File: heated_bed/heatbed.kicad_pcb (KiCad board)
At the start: 2 copper layers, 249.6 x 227 mm, 10 parts, among them P1 CONN_4

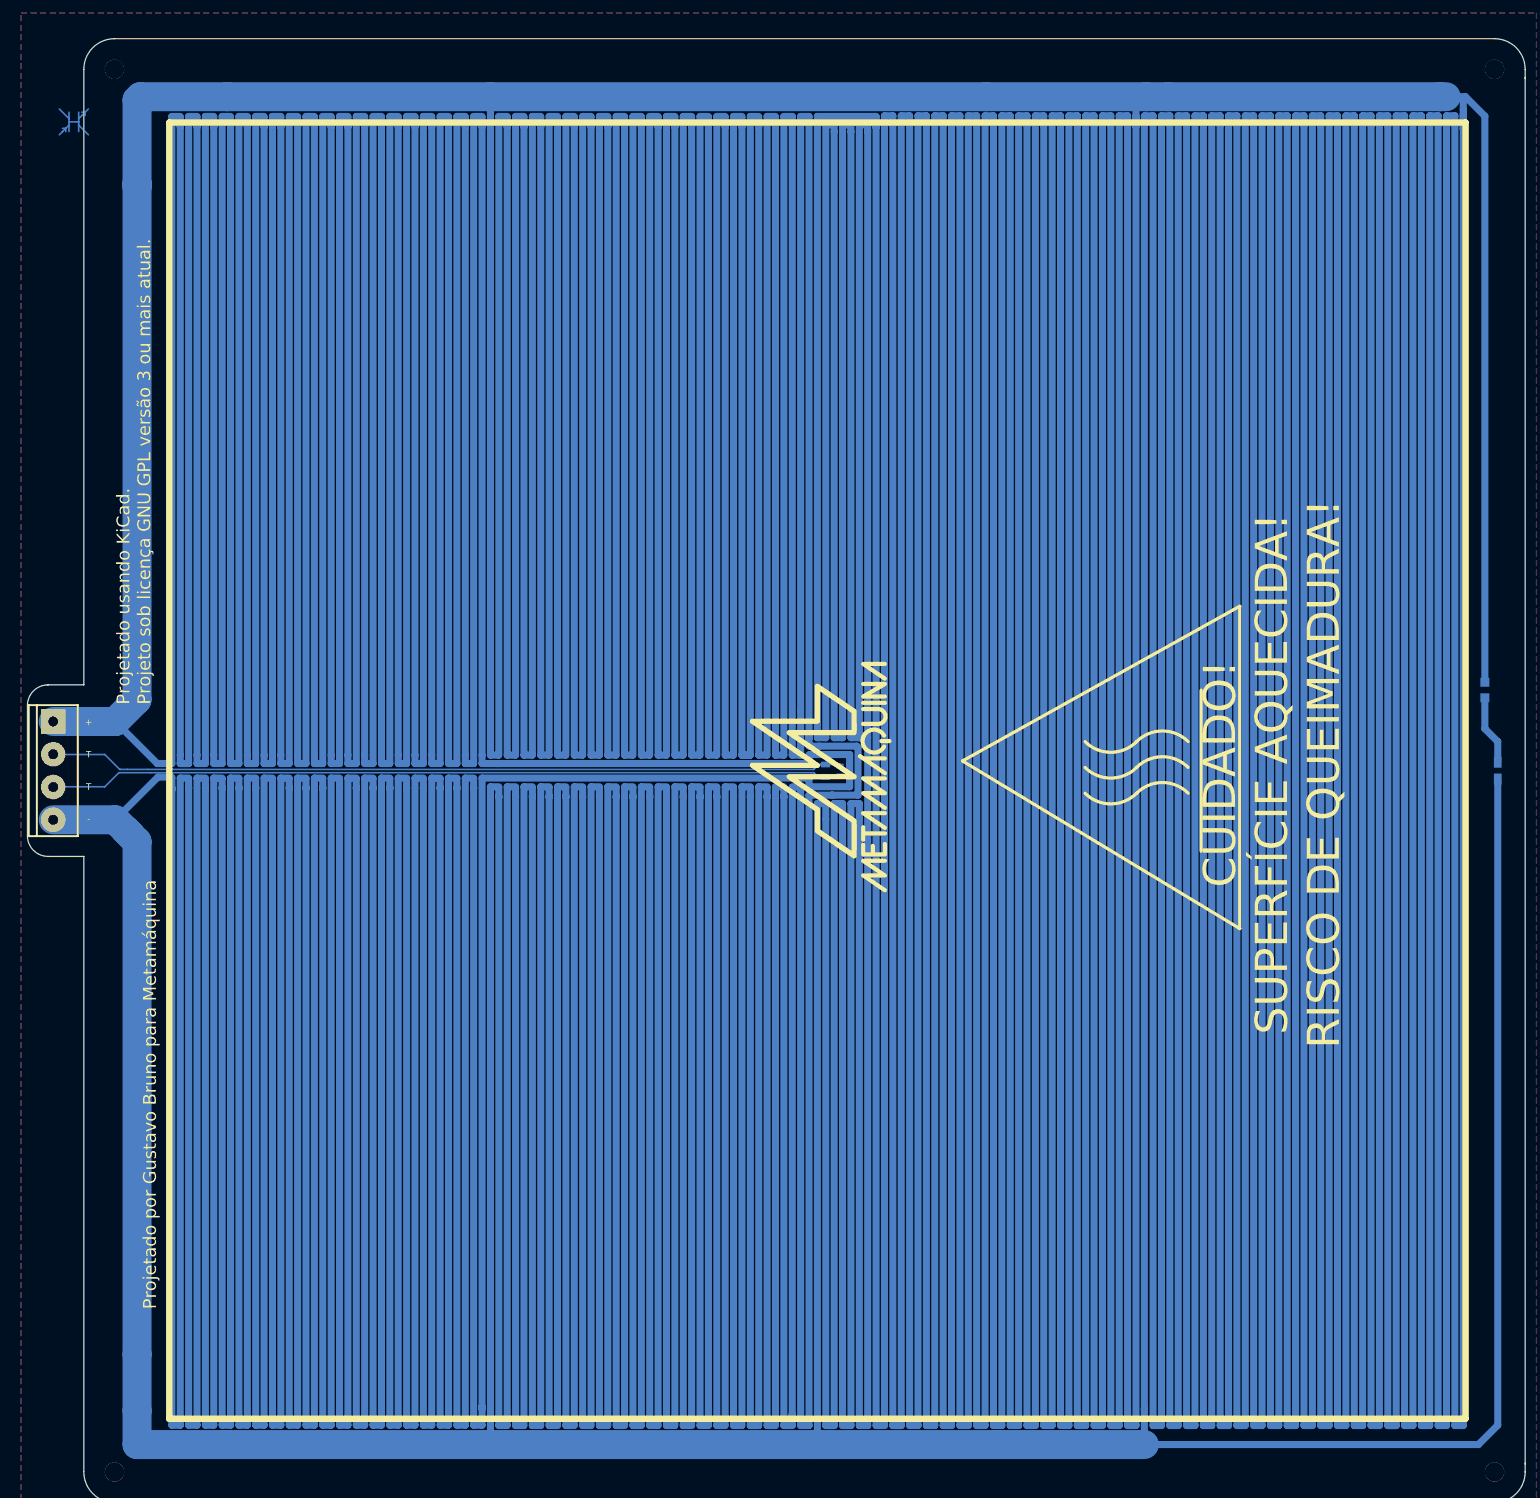
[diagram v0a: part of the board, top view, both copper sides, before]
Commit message: Correcoes apos prototipo fresado:
Bug que colava duas trilhas
Led avancado
Linha de distribuicao mais proxima
Textos do silk realinhados
Remoca do desenho de quente
Nome da placa
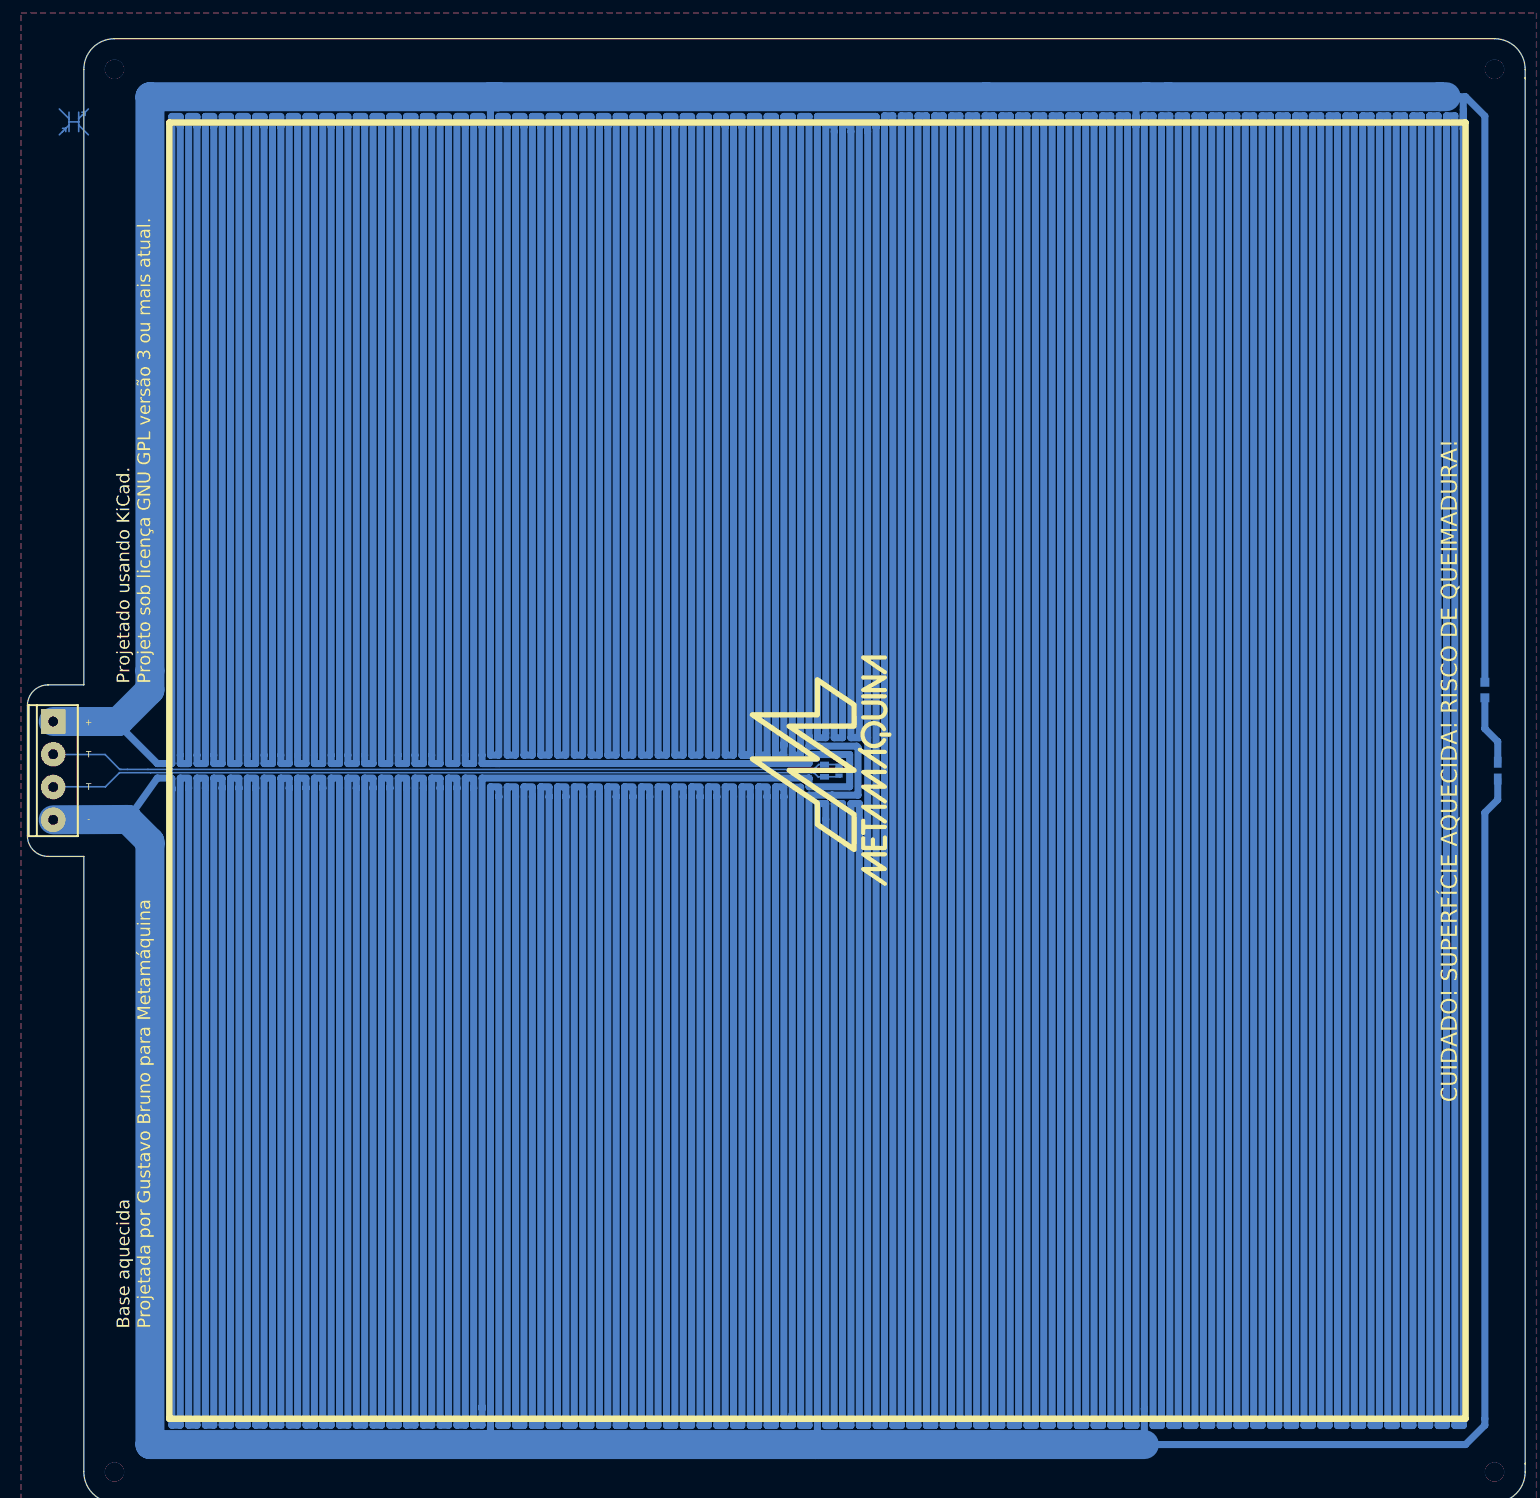
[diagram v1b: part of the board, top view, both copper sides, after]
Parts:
- moved VAL 1.00 mm to (199.0, 142.5)
- moved TH1 0.15 mm to (199.6, 142.5)
- moved TH2 0.15 mm to (201.8, 142.5)
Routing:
- net N-000005: track 32472.0 -> 32467.9 mm
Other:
- board text added: "Base aquecida Projetada por Gustavo Bruno para Metamáquina"
- board text removed: "Projetado por Gustavo Bruno para Metamáquina"
